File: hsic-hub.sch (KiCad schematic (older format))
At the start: 16 parts

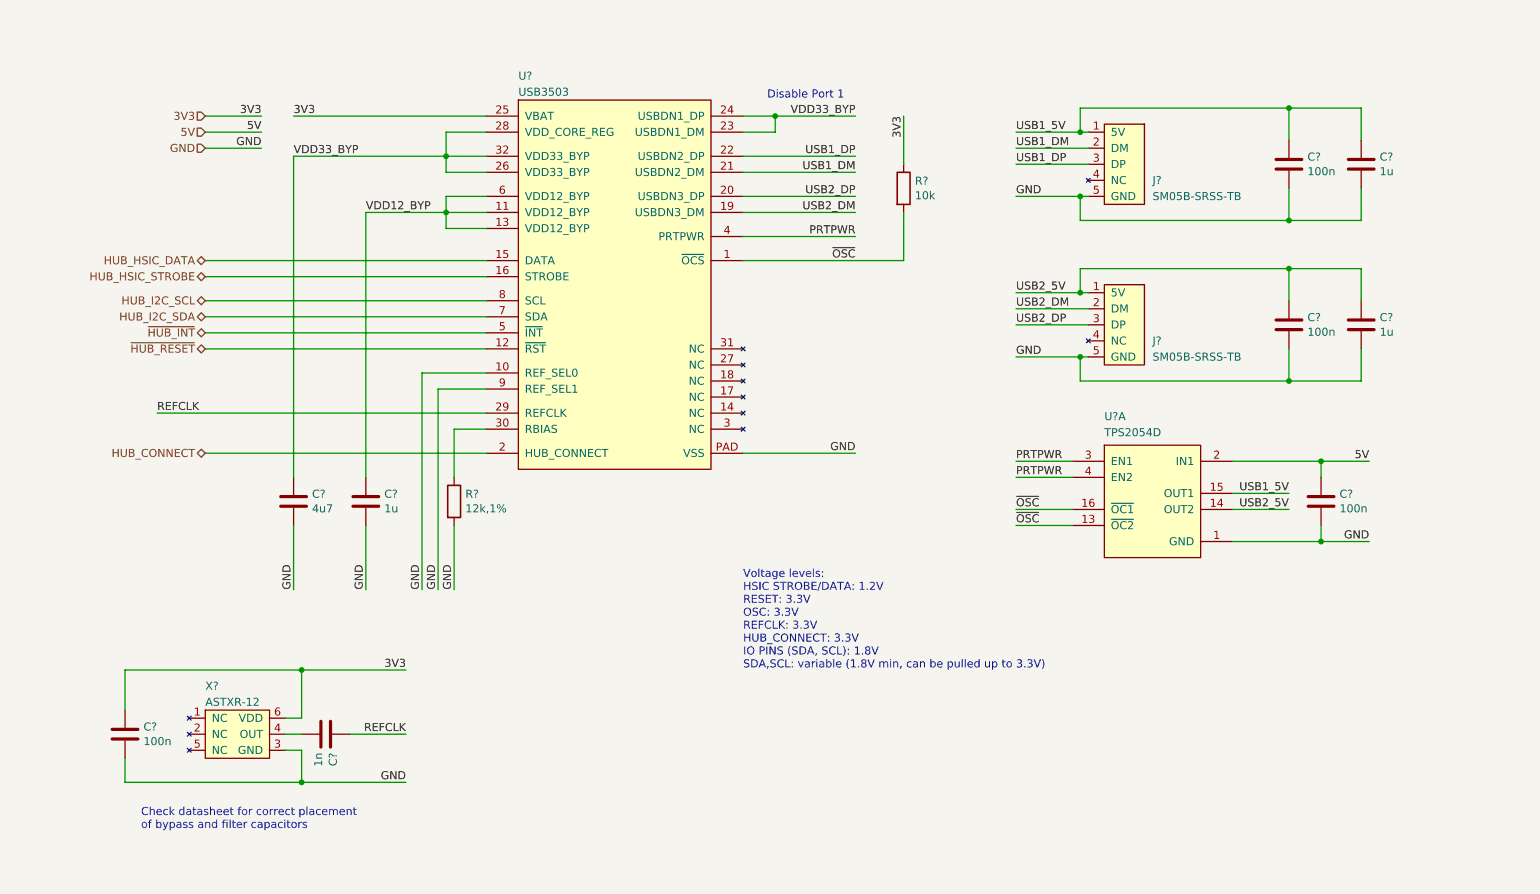
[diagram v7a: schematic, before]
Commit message: Minor adjustments to symbol library and HSIC schematic
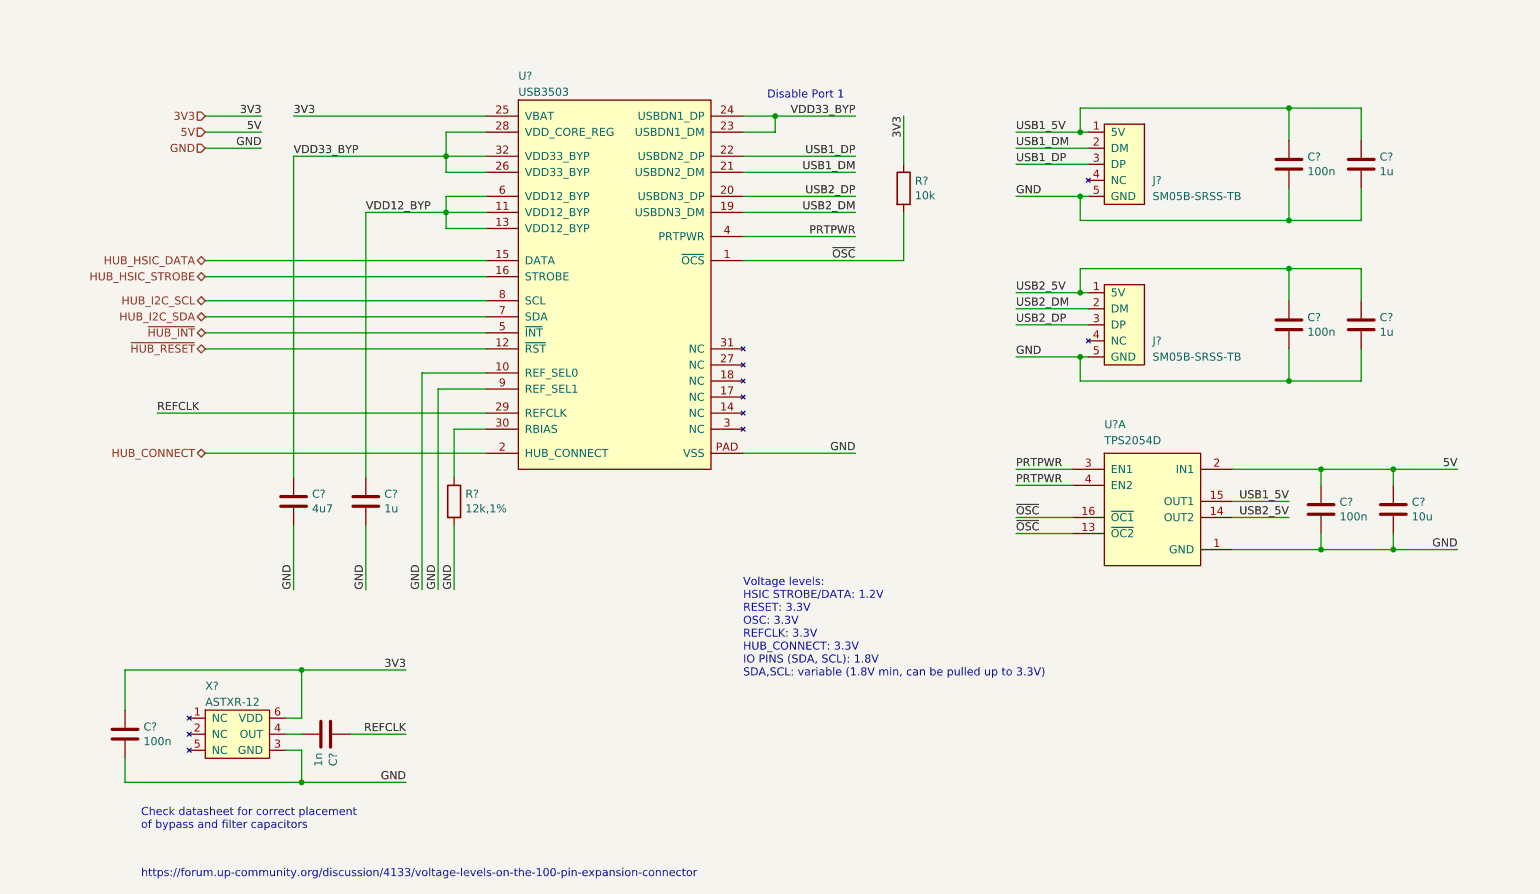
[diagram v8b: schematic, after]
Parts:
- added C?: 10u, symbol Device:C
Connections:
- net 5V: now also C?.1
- net GND: now also C?.2
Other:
- note added: "https://forum.up-community.org/discussion/4133/voltage-levels-on-the-100-pin-expansion-connector"
- moved on the sheet: C?, U?A
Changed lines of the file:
@@
 Wire Wire Line
 	1700 1400 2050 1400
-Text Label 8950 3450 2    50   ~ 0
+Text Label 9500 3500 2    50   ~ 0
 5V
 Wire Wire Line
@@
 L Device:C C?
 U 1 1 5E332CF8
-P 8650 3700
-F 0 "C?" H 8765 3746 50  0000 L CNN
-F 1 "100n" H 8765 3655 50  0000 L CNN
-F 2 "" H 8688 3550 50  0001 C CNN
-F 3 "~" H 8650 3700 50  0001 C CNN
-	1    8650 3700
-	1    0    0    -1
-$EndComp
-Text Label 8950 3950 2    50   ~ 0
+P 8650 3750
+F 0 "C?" H 8765 3796 50  0000 L CNN
+F 1 "100n" H 8765 3705 50  0000 L CNN
+F 2 "" H 8688 3600 50  0001 C CNN
+F 3 "~" H 8650 3750 50  0001 C CNN
+	1    8650 3750
+	1    0    0    -1
+$EndComp
+Text Label 9500 4000 2    50   ~ 0
 GND
 Text Label 6050 1300 3    50   ~ 0
@@
 	1    0    0    -1
 $EndComp
-Text Notes 5050 4750 0    50   ~ 0
+Text Notes 5050 4800 0    50   ~ 0
 Voltage levels:\nHSIC STROBE/DATA: 1.2V\nRESET: 3.3V\nOSC: 3.3V\nREFCLK: 3.3V\nHUB_CONNECT: 3.3V\nIO PINS (SDA, SCL): 1.8V\nSDA,SCL: variable (1.8V min, can be pulled up to 3.3V)
 Text Label 2950 4750 2    50   ~ 0
@@
 $EndComp
 Wire Wire Line
-	8100 3650 8450 3650
-Wire Wire Line
-	8100 3750 8450 3750
+	8100 3700 8450 3700
+Wire Wire Line
+	8100 3800 8450 3800
 Text Label 6750 1500 0    50   ~ 0
 USB1_DM
 Text Label 6750 1600 0    50   ~ 0
 USB1_DP
-Text Label 8450 3650 2    50   ~ 0
+Text Label 8450 3700 2    50   ~ 0
 USB1_5V
-Text Label 8450 3750 2    50   ~ 0
+Text Label 8450 3800 2    50   ~ 0
 USB2_5V
 Text Label 6750 1400 0    50   ~ 0
@@
 GND
 Wire Wire Line
-	6750 2800 7150 2800
-Wire Wire Line
 	6750 2600 7200 2600
 Wire Wire Line
@@
 Wire Wire Line
 	7150 2950 7150 2800
-Connection ~ 7150 2800
-Wire Wire Line
-	7150 2800 7200 2800
 Text Label 5750 1650 2    50   ~ 0
 USB1_DM
@@
 L Drone:TPS2054D U?
 U 1 1 5E4E09E8
-P 7600 3350
-F 0 "U?" H 7300 3500 50  0000 L BNN
-F 1 "TPS2054D" H 7300 3400 50  0000 L BNN
-F 2 "Package_SO:SOIC-16_3.9x9.9mm_P1.27mm" H 7300 3600 50  0001 L BNN
-F 3 "" H 7550 3350 50  0001 C CNN
-	1    7600 3350
+P 7600 3400
+F 0 "U?" H 7300 3550 50  0000 L BNN
+F 1 "TPS2054D" H 7300 3450 50  0000 L BNN
+F 2 "Package_SO:SOIC-16_3.9x9.9mm_P1.27mm" H 7300 3650 50  0001 L BNN
+F 3 "" H 7550 3400 50  0001 C CNN
+	1    7600 3400
 	1    0    0    -1
 $EndComp
@@
 Connection ~ 8450 2950
 Wire Wire Line
-	8100 3450 8650 3450
-Wire Wire Line
-	8100 3950 8650 3950
-Wire Wire Line
-	8650 3550 8650 3450
-Connection ~ 8650 3450
-Wire Wire Line
-	8650 3450 8950 3450
-Wire Wire Line
-	8650 3850 8650 3950
-Connection ~ 8650 3950
-Wire Wire Line
-	8650 3950 8950 3950
-Text Label 6750 3450 0    50   ~ 0
+	8100 3500 8650 3500
+Wire Wire Line
+	8100 4000 8650 4000
+Wire Wire Line
+	8650 3600 8650 3500
+Connection ~ 8650 3500
+Wire Wire Line
+	8650 3500 9100 3500
+Wire Wire Line
+	8650 3900 8650 4000
+Connection ~ 8650 4000
+Wire Wire Line
+	8650 4000 9100 4000
+Text Label 6750 3500 0    50   ~ 0
 PRTPWR
-Text Label 6750 3550 0    50   ~ 0
+Text Label 6750 3600 0    50   ~ 0
 PRTPWR
 Wire Wire Line
-	6750 3450 7100 3450
-Wire Wire Line
-	6750 3550 7100 3550
-Text Label 6750 3750 0    50   ~ 0
+	6750 3500 7100 3500
+Wire Wire Line
+	6750 3600 7100 3600
+Text Label 6750 3800 0    50   ~ 0
 ~OSC
-Text Label 6750 3850 0    50   ~ 0
+Text Label 6750 3900 0    50   ~ 0
 ~OSC
 Wire Wire Line
-	6750 3750 7100 3750
-Wire Wire Line
-	6750 3850 7100 3850
+	6750 3800 7100 3800
+Wire Wire Line
+	6750 3900 7100 3900
 Wire Wire Line
 	6050 1300 6050 1600
@@
 	-1   0    0    -1
 $EndComp
+$Comp
+L Device:C C?
+U 1 1 5E5A610D
+P 9100 3750
+F 0 "C?" H 9215 3796 50  0000 L CNN
+F 1 "10u" H 9215 3705 50  0000 L CNN
+F 2 "" H 9138 3600 50  0001 C CNN
+F 3 "~" H 9100 3750 50  0001 C CNN
+	1    9100 3750
+	1    0    0    -1
+$EndComp
+Wire Wire Line
+	9100 3600 9100 3500
+Connection ~ 9100 3500
+Wire Wire Line
+	9100 3500 9500 3500
+Wire Wire Line
+	9100 3900 9100 4000
+Connection ~ 9100 4000
+Wire Wire Line
+	9100 4000 9500 4000
+Wire Wire Line
+	6750 2800 7150 2800
+Connection ~ 7150 2800
+Wire Wire Line
+	7150 2800 7200 2800
+Text Notes 1300 6050 0    50   ~ 0
+https://forum.up-community.org/discussion/4133/voltage-levels-on-the-100-pin-expansion-connector
 $EndSCHEMATC
